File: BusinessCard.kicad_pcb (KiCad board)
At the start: 4 copper layers, 88.9 x 50.8 mm, 87 parts, among them Q1 2N3904, Q2 2N3904, Q3 2N3904, Q4 2N3904, U1 TLE2426, U2 TLV272, U3 TLV272, U4 LM393, U5 TLV272, U6 LM393, U7 FT232RL

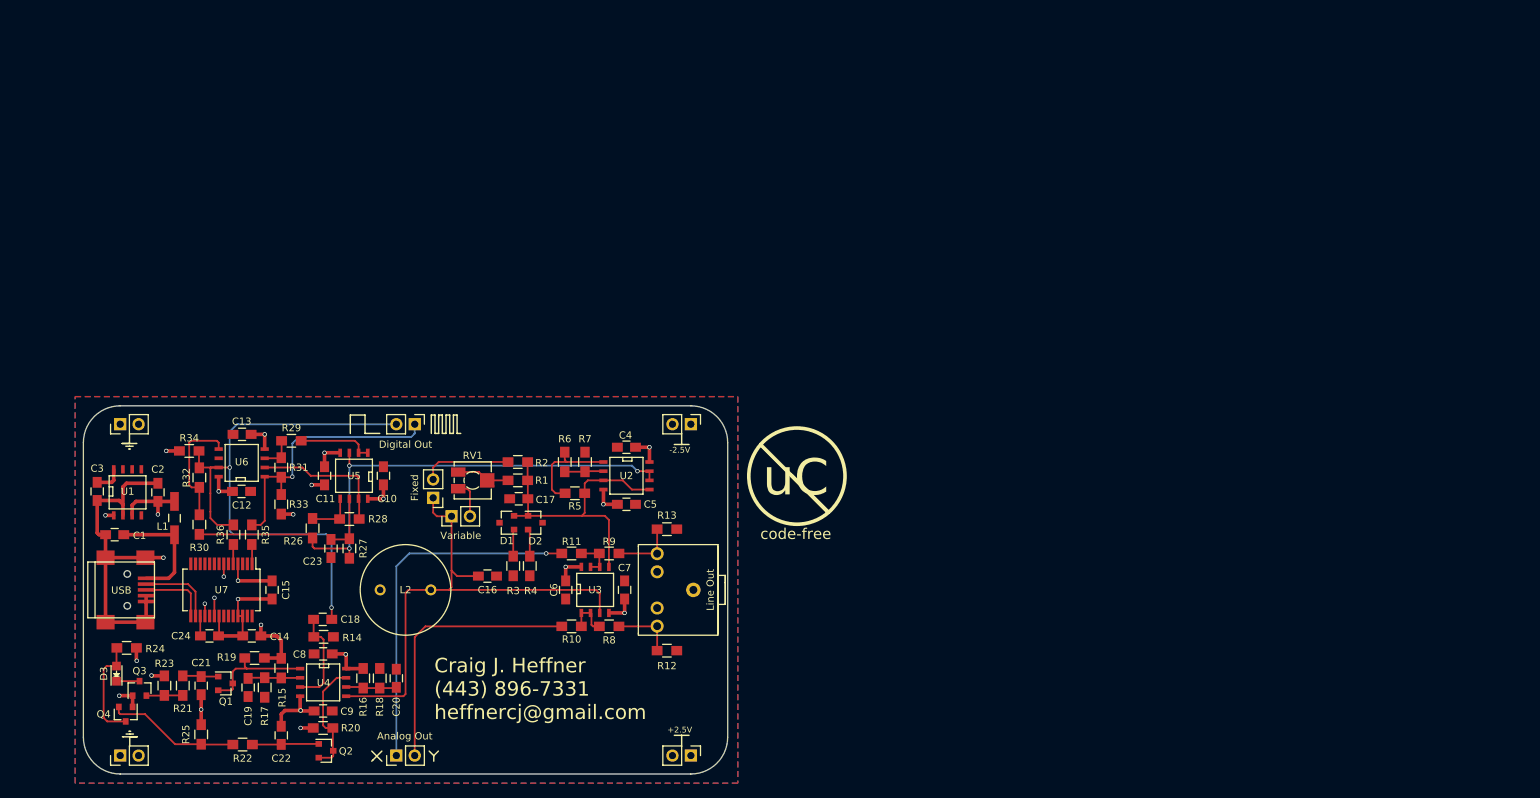
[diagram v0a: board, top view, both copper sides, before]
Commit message: Replaced GND with GNDREF; removed unecessary project specific footprint; new PCB outline ready for parts placement and routing.
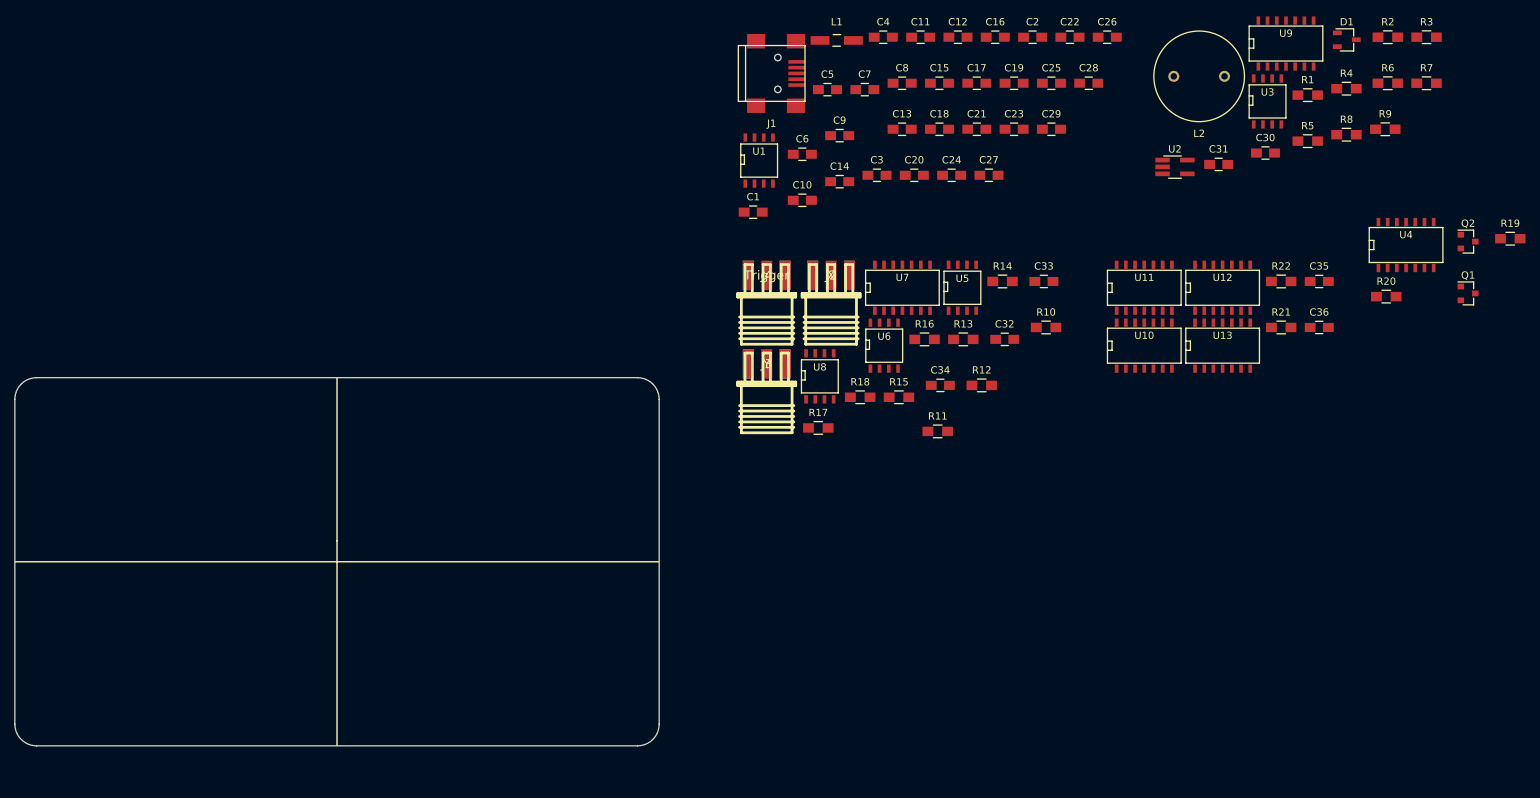
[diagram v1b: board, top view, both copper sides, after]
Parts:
- removed ? (x2): Ground, Pin_Headers:Pin_Header_Straight_1x02_Pitch2.54mm
- removed ?: +VDC, Pin_Headers:Pin_Header_Straight_1x02_Pitch2.54mm
- removed ?: -VDC, Pin_Headers:Pin_Header_Straight_1x02_Pitch2.54mm
- removed Analog Out: XY Out, Pin_Headers:Pin_Header_Straight_1x02_Pitch2.54mm
- removed D2: BAT54, TO_SOT_Packages_SMD:SOT-23
- removed D3: LED, LEDs:LED_0805
- removed Digital Out: DIGITAL_OUT, Pin_Headers:Pin_Header_Straight_1x02_Pitch2.54mm
- removed Fixed: Fixed, Pin_Headers:Pin_Header_Straight_1x02_Pitch2.54mm
- removed Line Out: XY Line Out, SJ1-352XN:SJ1-352XN
- removed Q3, Q4: 2N3904, TO_SOT_Packages_SMD:SOT-23
- removed R23, R25, R28, R30: 100k, Resistors_SMD:R_0805_HandSoldering
- removed R24: 470, Resistors_SMD:R_0805_HandSoldering
- removed R26, R35, R36: 10k, Resistors_SMD:R_0805_HandSoldering
- removed R27: 33k, Resistors_SMD:R_0805_HandSoldering
- removed R29, R33, R34: 1k, Resistors_SMD:R_0805_HandSoldering
- removed R31, R32: 1M, Resistors_SMD:R_0805_HandSoldering
- removed RV1: 1k, Potentiometers:Potentiometer_Trimmer_Vishay_TS53YJ
- removed USB: USB_OTG, Connect:USB_Mini-B
- removed Variable: Variable, Pin_Headers:Pin_Header_Straight_1x02_Pitch2.54mm
- added C25: 10uF, Capacitors_SMD:C_0805_HandSoldering, F.Cu at (248.1, 30.7)
- added C26: 10uF, Capacitors_SMD:C_0805_HandSoldering, F.Cu at (255.8, 24.3)
- added C27: 0.1uF, Capacitors_SMD:C_0805_HandSoldering, F.Cu at (239.5, 43.4)
- added C28: 10uF, Capacitors_SMD:C_0805_HandSoldering, F.Cu at (253.3, 30.7)
- added C29: 0.1uF, Capacitors_SMD:C_0805_HandSoldering, F.Cu at (248.1, 37.0)
- added C30: 0.1uF, Capacitors_SMD:C_0805_HandSoldering, F.Cu at (277.7, 40.3)
- added C31: 0.01uF, Capacitors_SMD:C_0805_HandSoldering, F.Cu at (271.2, 41.9)
- added C32: 1500pF, Capacitors_SMD:C_0805_HandSoldering, F.Cu at (241.7, 66.0)
- added C33: 1500pF, Capacitors_SMD:C_0805_HandSoldering, F.Cu at (247.1, 58.0)
- added C34: 1500pF, Capacitors_SMD:C_0805_HandSoldering, F.Cu at (232.8, 72.4)
- added C35: 0.1uF, Capacitors_SMD:C_0805_HandSoldering, F.Cu at (285.1, 58.0)
- added C36: 0.1uF, Capacitors_SMD:C_0805_HandSoldering, F.Cu at (285.1, 64.4)
- added J1: USB_OTG, Connect:USB_Mini-B, F.Cu at (209.5, 29.3)
- added J2: X, CON-SMA-EDGE:CON-SMA-EDGE, F.Cu at (217.7, 57.2)
- added J3: Y, CON-SMA-EDGE:CON-SMA-EDGE, F.Cu at (208.8, 69.4)
- added J4: Trigger, CON-SMA-EDGE:CON-SMA-EDGE, F.Cu at (208.8, 57.2)
- added U10: 74HC74, SMD_Packages:SOIC-14_N, F.Cu at (260.9, 66.8)
- added U11: 74HC74, SMD_Packages:SOIC-14_N, F.Cu at (260.9, 58.8)
- added U12: 74HC74, SMD_Packages:SOIC-14_N, F.Cu at (271.7, 58.8)
- added U13: 74HC74, SMD_Packages:SOIC-14_N, F.Cu at (271.7, 66.8)
- added U8: TLV272, SMD_Packages:SOIC-8-N, F.Cu at (216.2, 71.1)
- added U9: 74HC14, SMD_Packages:SOIC-14_N, F.Cu at (280.5, 25.1)
- C1, C14: value 10uF -> 0.1uF
- C10, C11, C12, C13, C17, C2, C4, C5, C6, C7, C8, C9: value 0.01uF -> 0.1uF
- C23: value 330pF -> 0.1uF
- D1: value BAT54 -> BAT54S; footprint TO_SOT_Packages_SMD:SOT-23 -> TO_SOT_Packages_SMD:TSOT-23
- R1: value 1k -> 1.37k
- R10: value 1k -> 15k
- R11: value 1k -> 10k
- R12, R13: value 2k -> 10k
- R14: value 100k -> 10k
- R16: value 100k -> 2.2k
- R17, R18: value 10k -> 2.2k
- R19, R20: value 1k -> 2.2k
- R2: value 1.43k -> 2.2k
- R21: value 10k -> 10M
- R22: value 10k -> 56k
- R4: value 2.2k -> 100k
- R6: value 1k -> 1M
- R8, R9: value 10k -> 1k
- U2: value TLV272 -> TLV271; footprint SMD_Packages:SOIC-8-N -> TO_SOT_Packages_SMD:TSOT-23-5_HandSoldering
- U3: value TLV272 -> LM311
- U4: value LM393 -> 74HC74; footprint SMD_Packages:SOIC-8-N -> SMD_Packages:SOIC-14_N
- U5: value TLV272 -> INA826
- U6: value LM393 -> TLV272
- U7: value FT232RL -> 4066; footprint Housings_SSOP:SSOP-28_5.3x10.2mm_Pitch0.65mm -> SMD_Packages:SOIC-14_N
- moved R19 182.7 mm to (311.4, 52.1)
- moved Q1 179.7 mm to (305.6, 59.7)
- moved Q2 172.5 mm to (305.6, 52.5)
- moved U4 161.2 mm to (297.1, 52.9), turned to 0 degrees
- moved R21 159.4 mm to (279.8, 64.4), turned to 0 degrees
- moved R20 158.3 mm to (294.3, 60.1), turned to 0 degrees
- moved R22 156.9 mm to (279.8, 58.0), turned to 0 degrees
- moved R3 145.6 mm to (299.9, 24.3), turned to 0 degrees
- moved C22 145.3 mm to (250.7, 24.3), turned to 0 degrees
- moved C2 136.0 mm to (245.5, 24.3), turned to 0 degrees
- moved C19 134.6 mm to (243.0, 30.7), turned to 0 degrees
- moved D1 133.7 mm to (288.9, 24.7), turned to 0 degrees
- moved R2 133.6 mm to (294.5, 24.3)
- moved C21 131.7 mm to (237.8, 37.0), turned to 0 degrees
- moved R4 130.5 mm to (288.8, 31.4), turned to 0 degrees
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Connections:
- C1 pad 1: Net-(C1-Pad1) -> +VDC
- C1 pad 2: -VDC -> GNDREF
- C10 pad 1: +VDC -> GNDREF
- C10 pad 2: GND -> -VDC
- C11 pad 1: GND -> +VDC
- C11 pad 2: -VDC -> GNDREF
- C12 pad 1: +VDC -> GNDREF
- C12 pad 2: GND -> -VDC
- C13 pad 1: GND -> +VDC
- C13 pad 2: -VDC -> GNDREF
- C14 pad 1: +VDC -> GNDREF
- C15 pad 2: -VDC -> GNDREF
- C16 pad 1: Y -> GNDREF
- C16 pad 2: GND -> -VDC
- C17 pad 1: X -> +VDC
- C17 pad 2: GND -> GNDREF
- C18 pad 1: X_ATTRACTOR -> GNDREF
- C18 pad 2: Net-(C18-Pad2) -> -VDC
- C19 pad 1: Net-(C19-Pad1) -> +VDC
- C19 pad 2: GND -> GNDREF
- C2 pad 1: +VDC -> GNDREF
- C20 pad 1: Net-(C20-Pad1) -> GNDREF
- C20 pad 2: GND -> -VDC
- C21 pad 1: Net-(C21-Pad1) -> +VDC
- C21 pad 2: -VDC -> GNDREF
- C22 pad 1: Net-(C22-Pad1) -> GNDREF
- C23 pad 1: Net-(C23-Pad1) -> +VDC
- C23 pad 2: GND -> GNDREF
- C24 pad 1: Net-(C24-Pad1) -> GNDREF
- C3 pad 1: Net-(C3-Pad1) -> +VDC
- C3 pad 2: -VDC -> GNDREF
- C4 pad 1: +VDC -> GNDREF
- C4 pad 2: GND -> -VDC
- C5 pad 1: GND -> +VDC
- C5 pad 2: -VDC -> GNDREF
- C6 pad 1: +VDC -> GNDREF
- C6 pad 2: GND -> -VDC
- C7 pad 1: GND -> +VDC
- C7 pad 2: -VDC -> GNDREF
- C8 pad 1: +VDC -> GNDREF
- C8 pad 2: GND -> -VDC
- C9 pad 1: GND -> +VDC
- C9 pad 2: -VDC -> GNDREF
- D1 pad 2: X -> Net-(D1-Pad2)
- D1 pad 3: (no net) -> Net-(C31-Pad1)
- L1 pad 1: Net-(C1-Pad1) -> Net-(C27-Pad1)
- L2 pad 1: GND -> GNDREF
- L2 pad 2: Y -> Net-(C30-Pad1)
- Q1 pad 1: Net-(C21-Pad1) -> Net-(Q1-Pad1)
- Q1 pad 2: Net-(Q1-Pad2) -> CLOCK_CYCLE_0
- Q1 pad 3: Net-(Q1-Pad2) -> CLOCK_CYCLE_0
- Q2 pad 1: Net-(C22-Pad1) -> Net-(Q1-Pad1)
- Q2 pad 2: Net-(Q2-Pad2) -> CLOCK_CYCLE_2
- Q2 pad 3: Net-(Q2-Pad2) -> CLOCK_CYCLE_2
- R1 pad 1: Net-(R1-Pad1) -> Net-(C30-Pad1)
- R1 pad 2: X -> Net-(C31-Pad1)
- R10 pad 1: Net-(R10-Pad1) -> COORDINATE
- R10 pad 2: Y_OUT -> Net-(R10-Pad2)
- R11 pad 1: Net-(R11-Pad1) -> Net-(R10-Pad2)
- R11 pad 2: X_OUT -> GNDREF
- R12 pad 1: GND -> Net-(R12-Pad1)
- R12 pad 2: Y_LINE -> GNDREF
- R13 pad 1: GND -> Net-(R12-Pad1)
- R13 pad 2: X_LINE -> Net-(R13-Pad2)
- R14 pad 1: Net-(C18-Pad2) -> Net-(R14-Pad1)
- R14 pad 2: GND -> Net-(R14-Pad2)
- R15 pad 1: Net-(C19-Pad1) -> Net-(R14-Pad2)
- R15 pad 2: +VDC -> GNDREF
- R16 pad 1: Net-(C20-Pad1) -> FRACTAL_X
- R16 pad 2: +VDC -> Net-(J2-Pad1)
- R17 pad 1: Net-(C19-Pad1) -> FRACTAL_Y
- R17 pad 2: GND -> Net-(J3-Pad1)
- R18 pad 1: Net-(C20-Pad1) -> FRACTAL_TRIGGER
- R18 pad 2: GND -> Net-(J4-Pad1)
- R19 pad 1: Net-(Q1-Pad2) -> CHUA_ATTRACTOR
- R19 pad 2: +VDC -> Net-(R19-Pad2)
- R2 pad 1: Net-(JP2-Pad2) -> Net-(D1-Pad2)
- R2 pad 2: X -> GNDREF
- R20 pad 1: Net-(Q2-Pad2) -> Net-(Q1-Pad1)
- R20 pad 2: +VDC -> -VDC
- R21 pad 1: Net-(C21-Pad1) -> +VDC
- R22 pad 1: Net-(C22-Pad1) -> Net-(C36-Pad1)
- R22 pad 2: Net-(Q4-Pad2) -> CLOCK
- R3 pad 2: GND -> GNDREF
- R4 pad 1: Net-(D2-Pad2) -> Net-(R4-Pad1)
- R4 pad 2: GND -> GNDREF
- R5 pad 1: X -> Net-(C31-Pad1)
- R6 pad 1: Net-(R5-Pad2) -> Net-(R6-Pad1)
- R6 pad 2: Net-(R6-Pad2) -> Net-(R4-Pad1)
- R7 pad 1: Net-(R6-Pad2) -> Net-(R5-Pad2)
- R7 pad 2: GND -> Net-(R7-Pad2)
- R8 pad 1: Net-(R10-Pad1) -> Net-(R7-Pad2)
- R8 pad 2: Y_LINE -> GNDREF
- R9 pad 1: Net-(R11-Pad1) -> +VDC
- R9 pad 2: X_LINE -> Net-(R6-Pad1)
- U1 pad 1: GND -> GNDREF
- U1 pad 8: Net-(C3-Pad1) -> Net-(C29-Pad1)
- U2 pad 2: Net-(R6-Pad2) -> -VDC
- U2 pad 3: X -> Net-(C31-Pad1)
- U2 pad 4: -VDC -> Net-(R7-Pad2)
- U2 pad 5: X -> +VDC
- U3 pad 1: Net-(R10-Pad1) -> -VDC
- U3 pad 2: Net-(R10-Pad1) -> Net-(R4-Pad1)
- U3 pad 3: Y -> Net-(C31-Pad1)
- U3 pad 5: X -> Net-(U3-Pad5)
- U3 pad 6: Net-(R11-Pad1) -> Net-(U3-Pad6)
- U3 pad 7: Net-(R11-Pad1) -> Net-(R6-Pad1)
- U4 pad 1: Net-(Q1-Pad2) -> +VDC
- U4 pad 2: Net-(C19-Pad1) -> Net-(R19-Pad2)
- U4 pad 3: Net-(C18-Pad2) -> Net-(Q1-Pad1)
- U4 pad 4: -VDC -> +VDC
- U4 pad 5: Y -> COORDINATE
- U4 pad 6: Net-(C20-Pad1) -> Net-(U4-Pad6)
- U4 pad 7: Net-(Q2-Pad2) -> -VDC
- U4 pad 8: +VDC -> Net-(U4-Pad8)
- U5 pad 1: Net-(R29-Pad1) -> Net-(R10-Pad2)
- U5 pad 2: Net-(R29-Pad1) -> Net-(U5-Pad2)
- U5 pad 3: X_BUFFERED -> Net-(U5-Pad3)
- U5 pad 4: -VDC -> Net-(R12-Pad1)
- U5 pad 5: Net-(R26-Pad2) -> -VDC
- U5 pad 6: Net-(C23-Pad1) -> GNDREF
- U5 pad 7: Net-(R28-Pad2) -> Net-(R14-Pad1)
- U6 pad 1: X_OSCILLATION -> Net-(U6-Pad1)
- U6 pad 2: Net-(R28-Pad2) -> Net-(U6-Pad1)
- U6 pad 3: Net-(R29-Pad2) -> Net-(R14-Pad2)
- U6 pad 5: Net-(R30-Pad2) -> Net-(C32-Pad1)
- U6 pad 6: GND -> Net-(R13-Pad2)
- U6 pad 7: X_ATTRACTOR -> Net-(R13-Pad2)
- U7 pad 1: Net-(R35-Pad1) -> Net-(U6-Pad1)
- U7 pad 11: Net-(U7-Pad11) -> Net-(U6-Pad1)
- U7 pad 12: Net-(U7-Pad12) -> CLOCK_CYCLE_3
- U7 pad 13: Net-(U7-Pad13) -> CLOCK_CYCLE_1
- U7 pad 14: Net-(U7-Pad14) -> +VDC
- U7 pad 3: Net-(U7-Pad3) -> Net-(C32-Pad1)
- U7 pad 4: +VDC -> FRACTAL_X
- U7 pad 5: Net-(R36-Pad1) -> CLOCK_CYCLE_0
- U7 pad 6: Net-(U7-Pad6) -> CLOCK_CYCLE_2
- U7 pad 8: Net-(U7-Pad8) -> FRACTAL_Y
- U7 pad 9: Net-(U7-Pad9) -> Net-(C32-Pad1)
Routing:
- net -VDC: track 101.9 -> 0.00 mm, vias 12 -> 0
- net X_ATTRACTOR: track 80.9 -> 0.00 mm, vias 2 -> 0
- net X_BUFFERED: track 79.8 -> 0.00 mm, vias 3 -> 0
- net Y: track 71.2 -> 0.00 mm
- net +VDC: track 57.8 -> 0.00 mm, vias 13 -> 0
- net X_OUT: track 49.7 -> 0.00 mm, vias 1 -> 0
- net X: track 41.5 -> 0.00 mm
- net X_OSCILLATION: track 37.7 -> 0.00 mm, vias 1 -> 0
- net Y_OUT: track 37.3 -> 0.00 mm
- net Net-(R28-Pad2): track 19.3 -> 0.00 mm
- net Net-(Q4-Pad2): track 18.4 -> 0.00 mm
- net Net-(C1-Pad1): track 16.6 -> 0.00 mm
- net Net-(R30-Pad2): track 16.3 -> 0.00 mm
- net Net-(Q2-Pad2): track 16.1 -> 0.00 mm
- net Net-(Q1-Pad2): track 15.5 -> 0.00 mm
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- removed copper zone on Vcc.Cu, net +VDC
- removed copper zone on Vee.Cu, net -VDC
- removed copper zone on B.Cu, net GND
- removed copper zone on F.Cu, net GND
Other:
- outline, holes or cut-outs redrawn
- net class Default: clearance 0.2 -> 0.25
- rule pad_to_mask_clearance: 0.2 -> 0
- rule trace_clearance: 0.2 -> 0.25
- rule trace_min: 0.2 -> 0.25
- board text removed: "+2.5V"
- board text removed: "-2.5V"
- board text removed: "Craig J. Heffner (443) 896-7331 heffnercj@gmail.com"
- board text removed: "code-free"
- board text removed: "http://www.analogzoo.com/businesscard"
- board text removed: "uC"

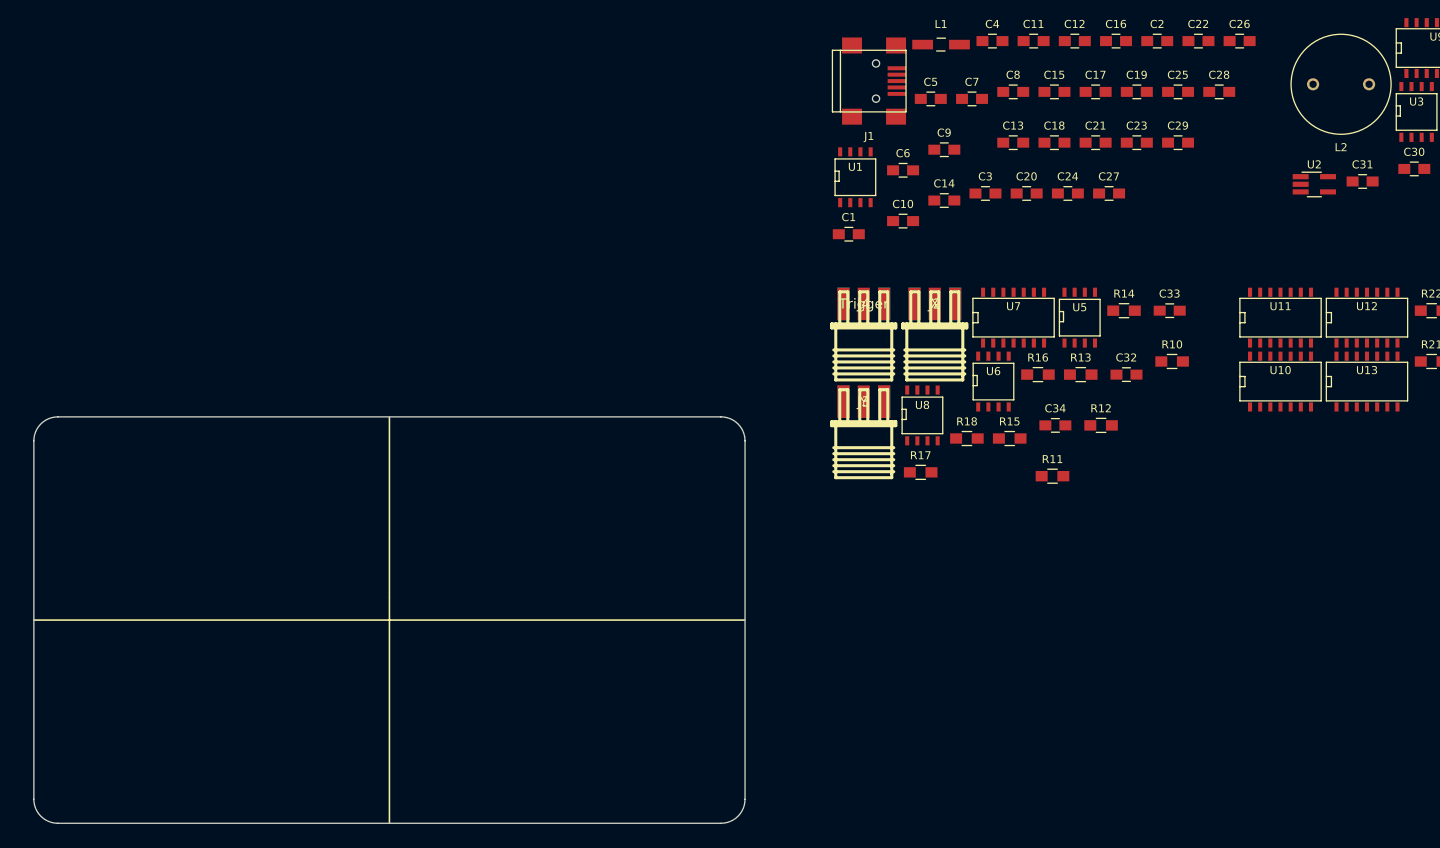
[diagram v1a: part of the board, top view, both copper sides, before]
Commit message: Power, output buffer, and analog switch placed.
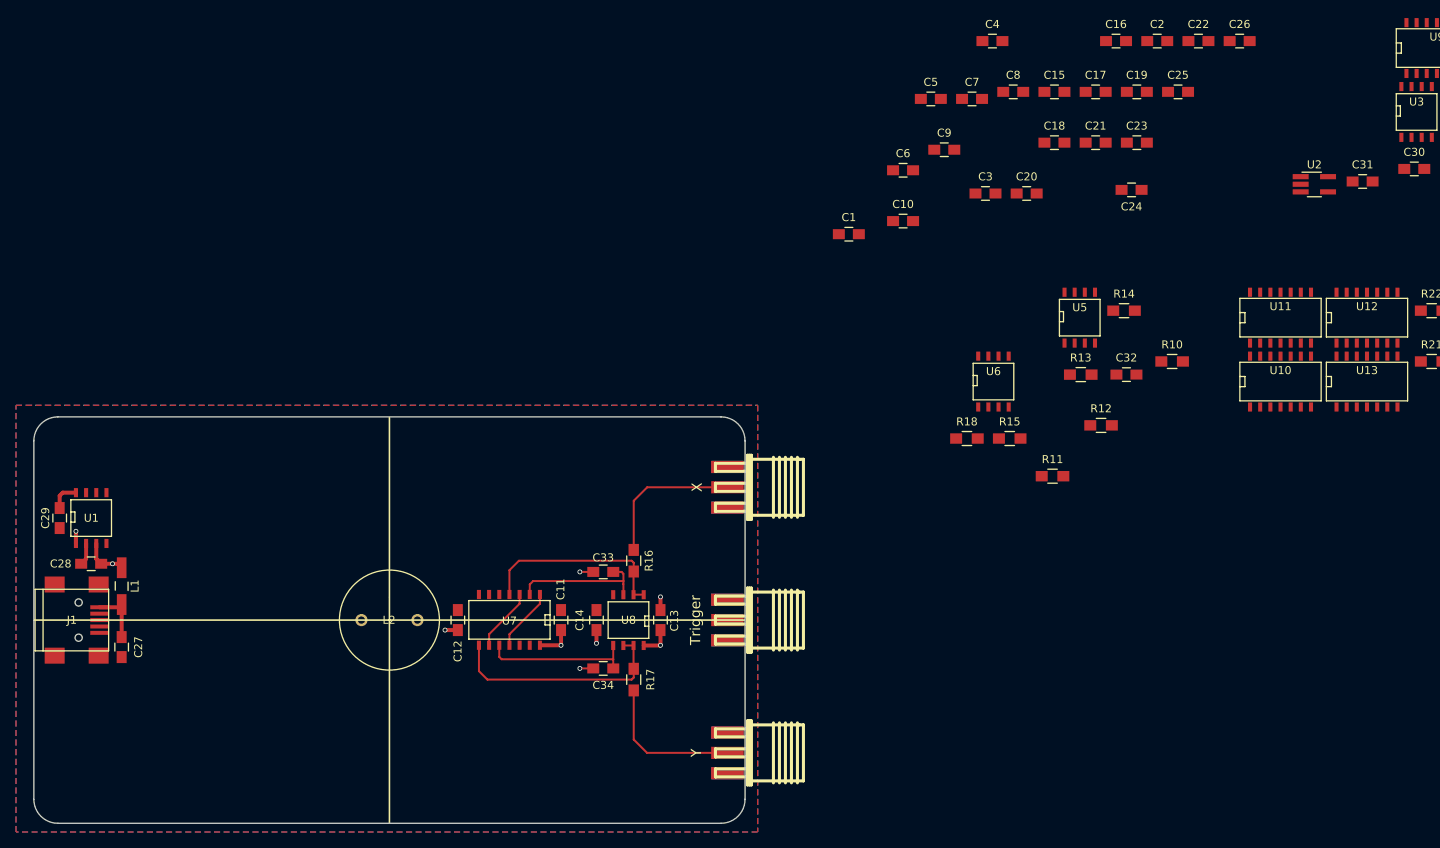
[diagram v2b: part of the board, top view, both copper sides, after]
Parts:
- moved C28 152.8 mm to (112.3, 89.7), turned to 180 degrees
- moved C29 147.5 mm to (108.3, 83.9), turned to 270 degrees
- moved L2 136.5 mm to (149.6, 96.7), turned to 180 degrees
- moved C27 135.8 mm to (116.1, 100.1), turned to 270 degrees
- moved L1 122.8 mm to (116.1, 92.5), turned to 90 degrees
- moved J1 120.3 mm to (109.8, 96.7)
- moved C12 105.8 mm to (158.1, 96.7), turned to 90 degrees
- moved U1 104.6 mm to (112.3, 83.9)
- moved C11 93.4 mm to (171.0, 96.7), turned to 90 degrees
- moved C33 78.0 mm to (176.3, 90.7), turned to 180 degrees
- moved C13 74.2 mm to (183.4, 96.7), turned to 90 degrees
- moved U7 73.6 mm to (164.6, 96.8), turned to 180 degrees
- moved C14 68.1 mm to (175.4, 96.7), turned to 90 degrees
- moved C34 64.2 mm to (176.3, 102.7), turned to 180 degrees
- moved R16 55.6 mm to (180.1, 89.3), turned to 90 degrees
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- renumbered J4 to Trigger, J2 to X, J3 to Y
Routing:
- net FRACTAL_Y: track 0.00 -> 28.4 mm
- net FRACTAL_X: track 0.00 -> 24.4 mm
- net Net-(C34-Pad1): track 0.00 -> 18.7 mm
- net Net-(J2-Pad1): track 0.00 -> 18.6 mm
- net Net-(J3-Pad1): track 0.00 -> 18.5 mm
- net Net-(C33-Pad1): track 0.00 -> 17.1 mm
- net +VDC: track 0.00 -> 14.1 mm, vias 0 -> 3
- net GNDREF: track 0.00 -> 9.77 mm, vias 0 -> 6
- net Net-(U6-Pad1): track 0.00 -> 7.93 mm
- net Net-(C32-Pad1): track 0.00 -> 7.93 mm
- net Net-(C27-Pad1): track 0.00 -> 6.99 mm
- net Net-(C29-Pad1): track 0.00 -> 3.73 mm
- net -VDC: track 0.00 -> 2.79 mm
- added copper zone on B.Cu, net +VDC
- added copper zone on F.Cu, net -VDC
- added copper zone on GND1.Cu, net GNDREF
- added copper zone on GND2.Cu, net GNDREF
